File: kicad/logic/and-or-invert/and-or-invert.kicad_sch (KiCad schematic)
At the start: 10 parts, among them Q1 BSS8402DW-7-F, Q2 BSS8402DW-7-F, Q3 BSS8402DW-7-F

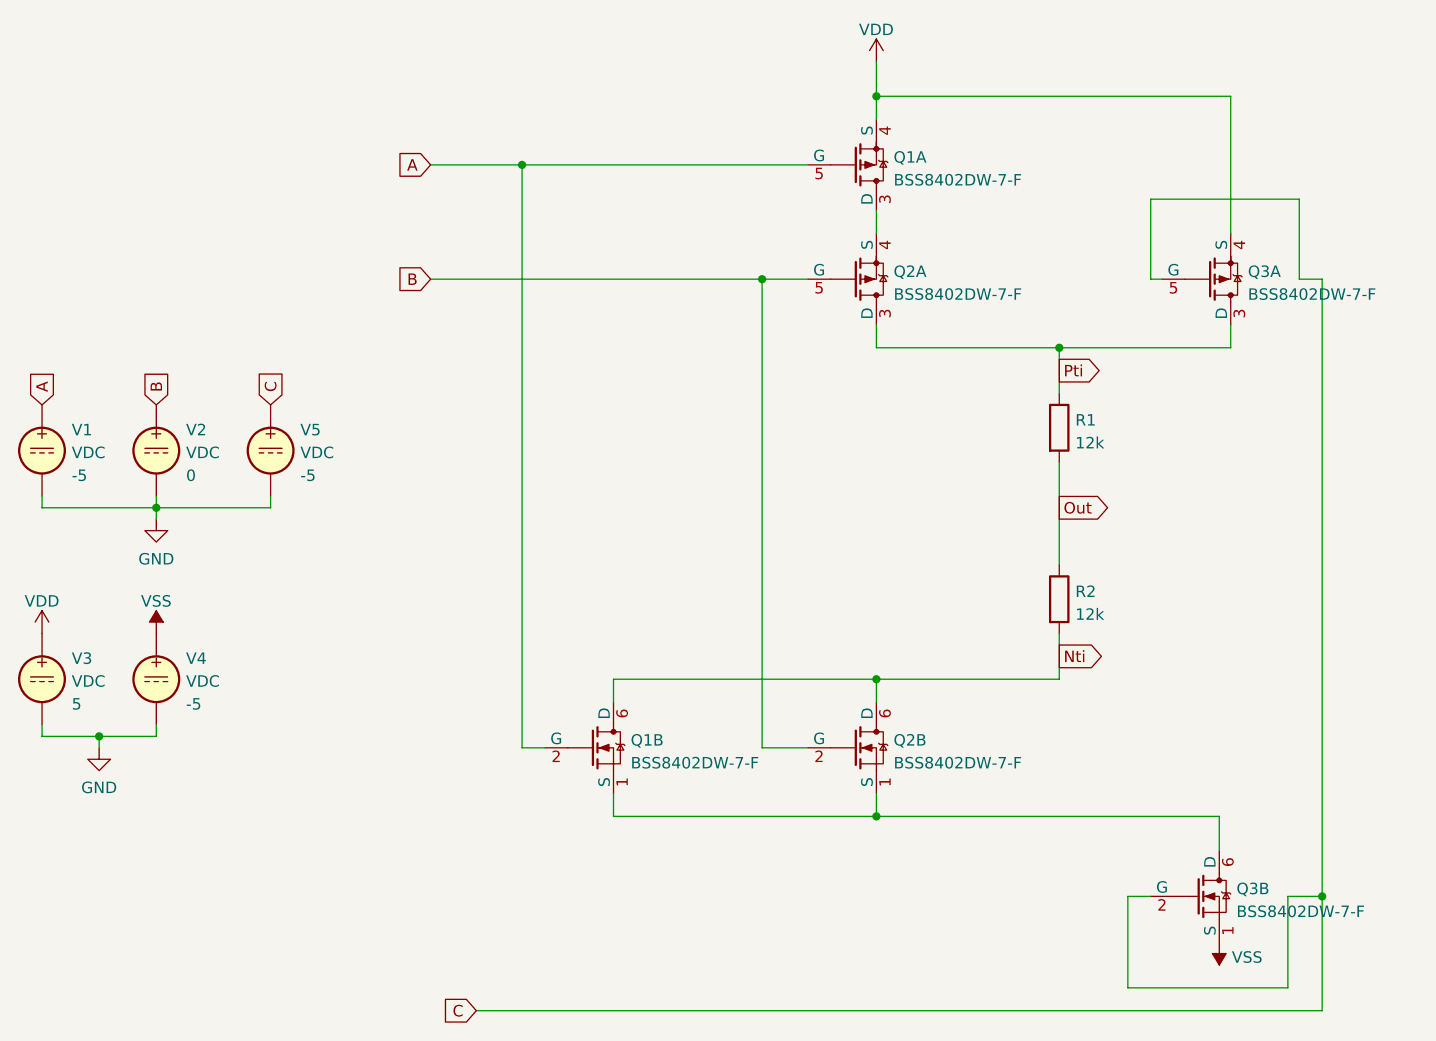
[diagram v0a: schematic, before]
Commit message: update to kicad 9
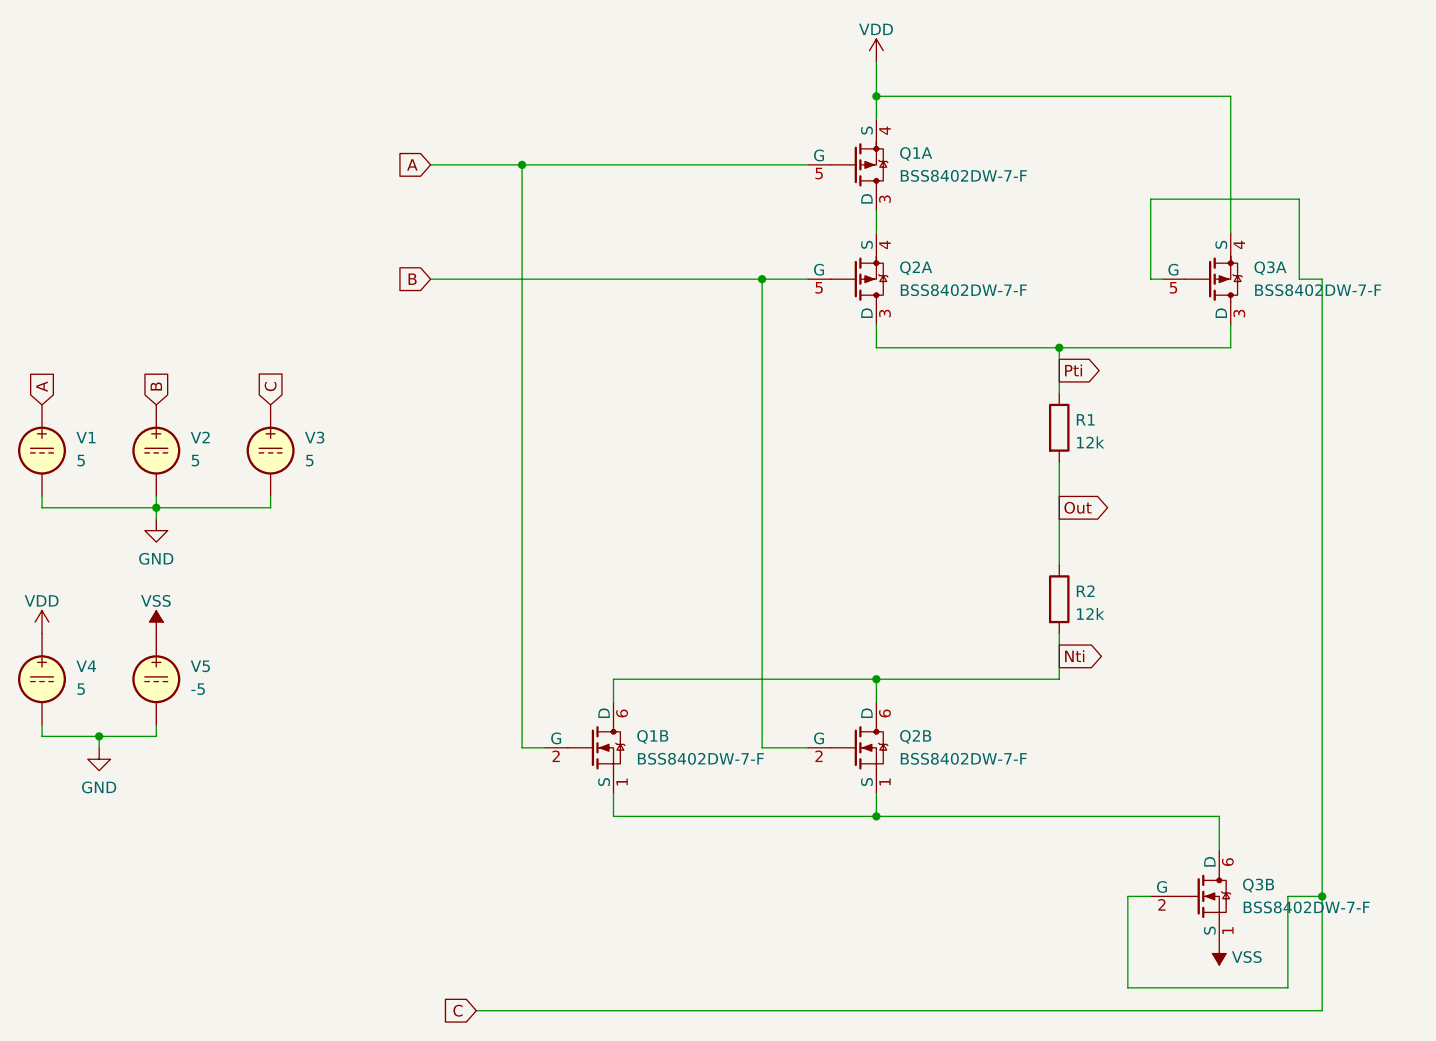
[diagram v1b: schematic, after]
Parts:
- Q1, Q2, Q3: Spice_Lib_File ${TRITIUM_LIB}/TritiumSpice.lib -> (none); Spice_Model BSS8402DW -> (none); Spice_Primitive X -> (none)
- V1, V4: value VDC -> 5; Spice_Model -5 -> (none); Spice_Netlist_Enabled Y -> (none); Spice_Primitive V -> (none)
- V2: value VDC -> 5; Spice_Model 0 -> (none); Spice_Netlist_Enabled Y -> (none); Spice_Primitive V -> (none)
- V3: value VDC -> 5; Spice_Model 5 -> (none); Spice_Netlist_Enabled Y -> (none); Spice_Primitive V -> (none)
- V5: value VDC -> -5; Spice_Model -5 -> (none); Spice_Netlist_Enabled Y -> (none); Spice_Primitive V -> (none)
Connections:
- net C: now also V3.1; no longer V5.1
- net VDD: now also V4.1; no longer V3.1
- net VSS: now also V5.1; no longer V4.1
